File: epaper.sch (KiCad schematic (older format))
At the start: 6 parts, among them CON1 SD_Card, P1 USB_OTG, U1 ch340g, U2 LTC4080, U3 ESP-12E, U4 TCA8418RTWR

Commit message: keypad
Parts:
- added C?: 100nf, symbol C
- added C?: 10pF, symbol C
- added C? (x3): 4.7uf, symbol C
- added L?: NRG4026T100M, symbol INDUCTOR
- added R?: 10k, symbol R
- added R? (x2): 470, symbol R
- added R?: 806, symbol R
- added R? (x2): R, symbol R
- added R? (x3): 0, symbol R
- added SW? (x40): butt, symbol SW_PUSH_SMALL_H
- added Y?: 12mhz, symbol Crystal
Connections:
- net labels added: +3V3, +5V, +BATT, COL0, COL1, COL2, COL3, COL4, COL5, COL6, COL7, COL8, COL9, ROW0, ROW1, ROW2, ROW3, RXD0, SCL, SDA, TXD0
- wire segments 13 -> 144
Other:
- moved on the sheet: CON1, P1, U1, U2

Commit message: display conn and ltc4080
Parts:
- added C?: 100nf, symbol C
- added C?: 10uf, symbol C
- added P?: Sharp Memory LCD, symbol CONN_01X10
- added R?: 0, symbol R
- C?: value 10pF -> 10pf
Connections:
- net labels added: CS_LCD
- net labels removed: VCC
- wire segments 144 -> 244

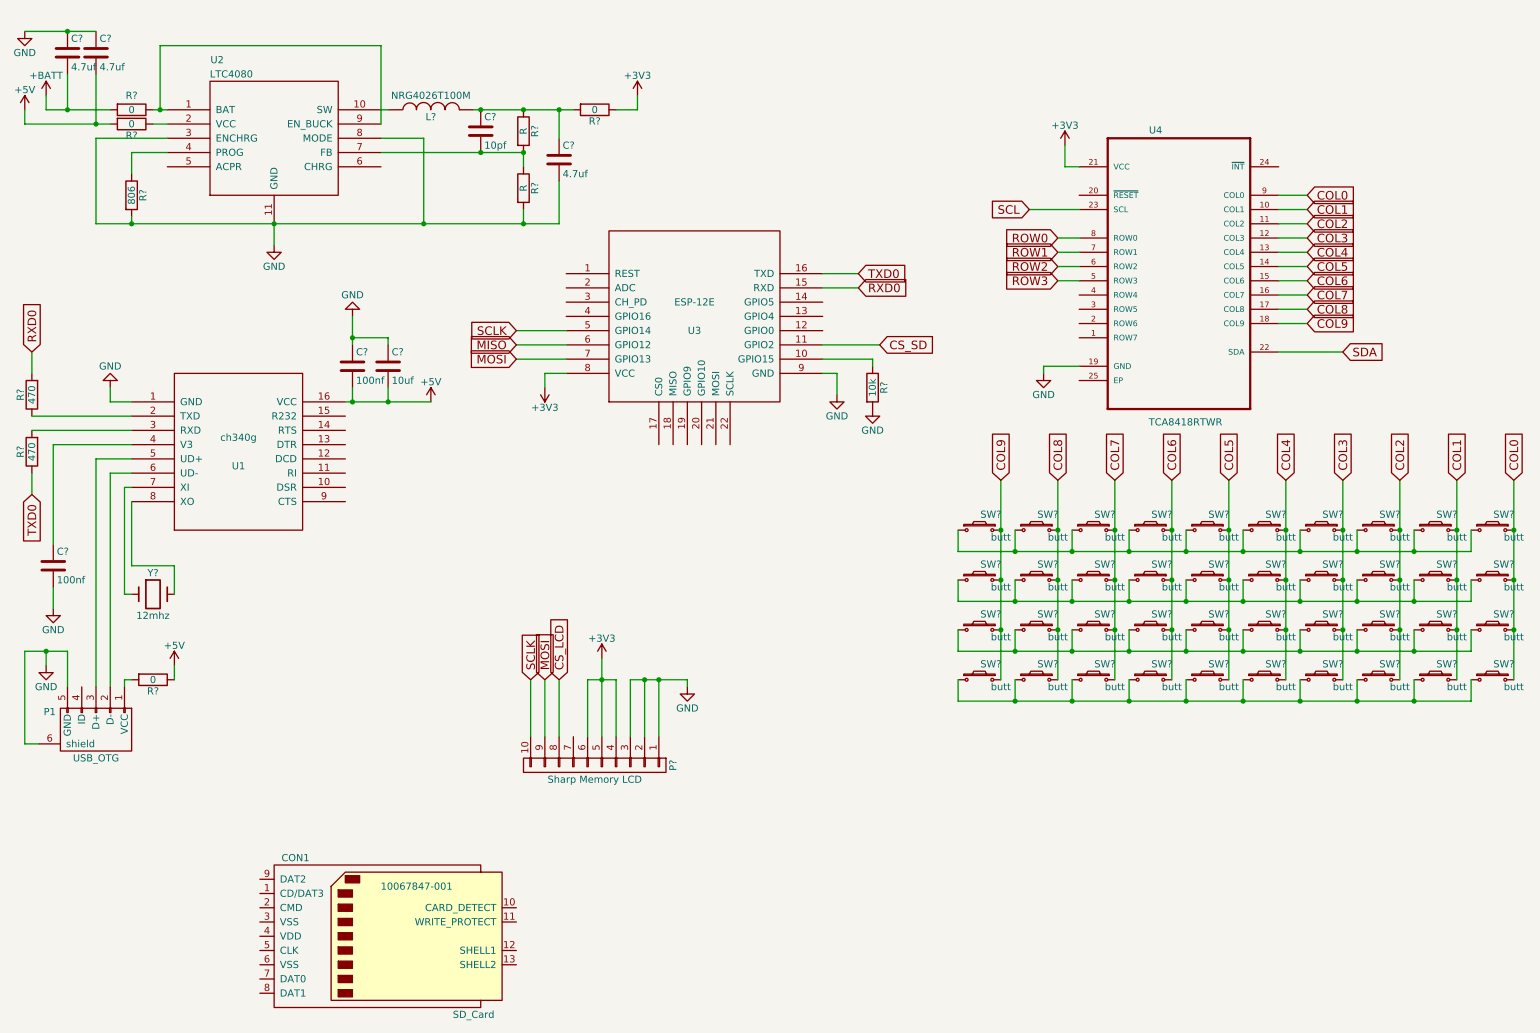
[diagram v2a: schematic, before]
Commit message: usb to rs232
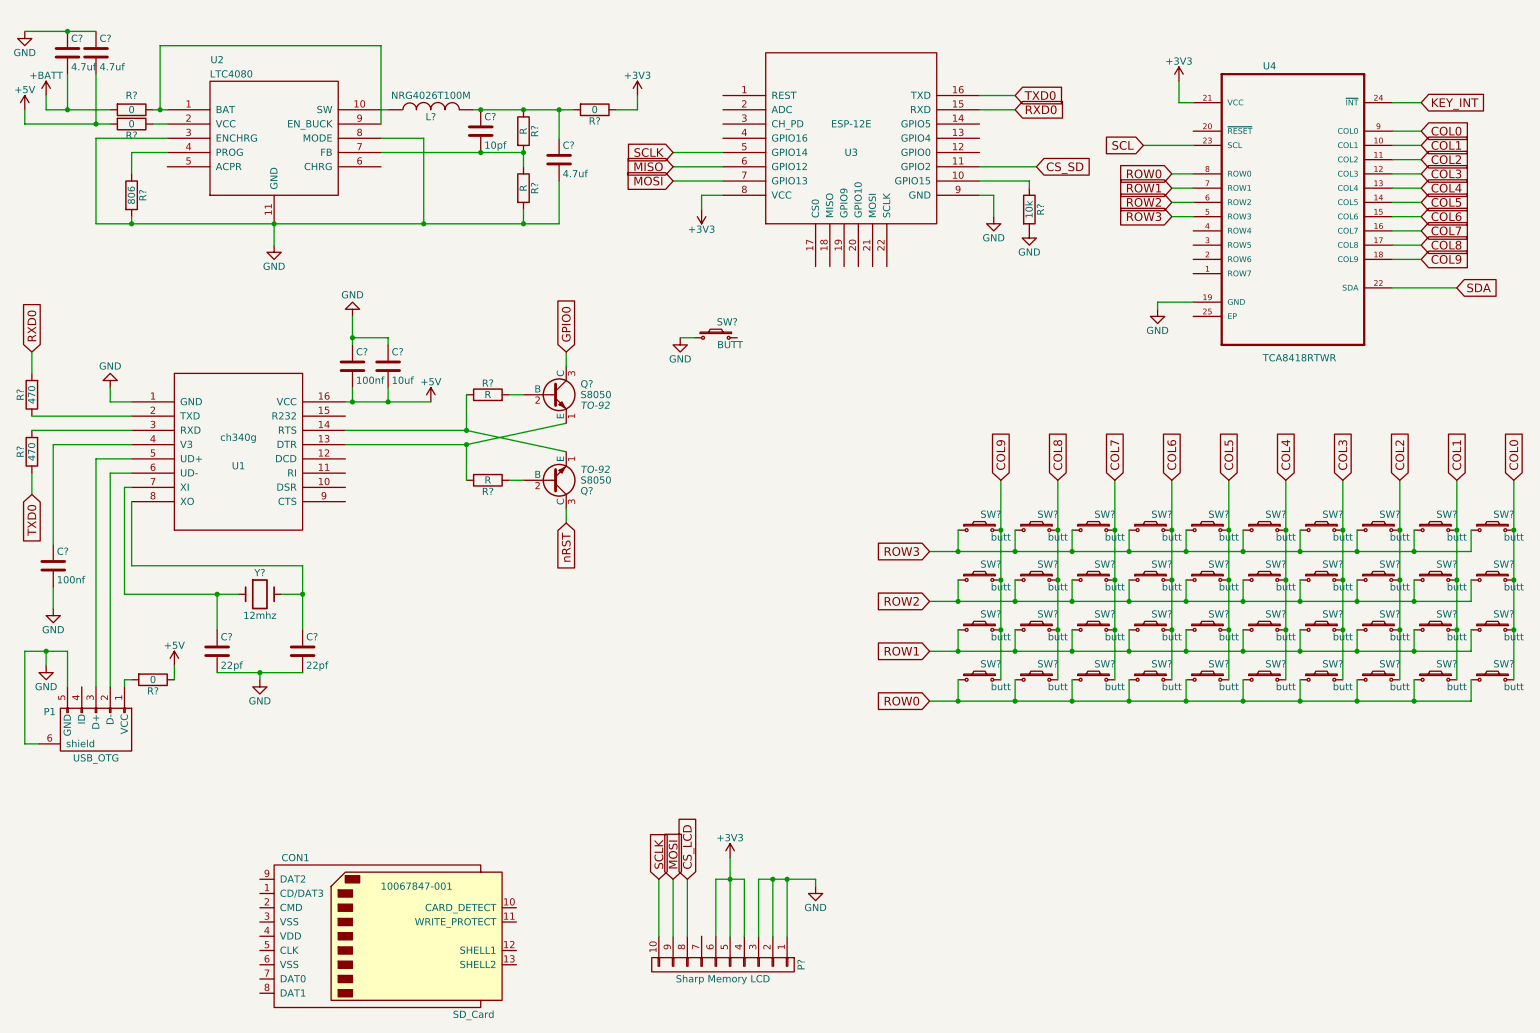
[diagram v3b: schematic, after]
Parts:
- added C? (x2): 22pf, symbol C
- added Q? (x2): S8050, TO-92, symbol S8050
- added R? (x2): R, symbol R
- added SW?: BUTT, symbol SW_PUSH_SMALL_H
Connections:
- net GND: now also C?.2, C?.2, SW?.1
- net ROW0: now also SW?.1, SW?.1, SW?.1, SW?.1, SW?.1, SW?.1, SW?.1, SW?.1, SW?.1, SW?.1
- net ROW1: now also SW?.1, SW?.1, SW?.1, SW?.1, SW?.1, SW?.1, SW?.1, SW?.1, SW?.1, SW?.1
- net ROW2: now also SW?.1, SW?.1, SW?.1, SW?.1, SW?.1, SW?.1, SW?.1, SW?.1, SW?.1, SW?.1
- net ROW3: now also SW?.1, SW?.1, SW?.1, SW?.1, SW?.1, SW?.1, SW?.1, SW?.1, SW?.1, SW?.1
- net KEY_INT: now reaches U4.24 (~INT)
- net at U1.13 (DTR): now also Q?.1 (E), R?.2
- net at U1.14 (RTS): now also Q?.1 (E), R?.1
- net at U1.7 (XI), Y?.1: now also C?.1
- net at U1.8 (XO), Y?.2: now also C?.1
- new net: Q?.2 (B), R?.2
- new net: Q?.2 (B), R?.1
- new net GPIO0: Q?.3 (C)
- new net nRST: Q?.3 (C)
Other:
- moved on the sheet: P?, R?, U3, U4, Y?

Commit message: before append new sheet
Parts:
- removed CON1: SD_Card, 10067847-001, symbol SD_Card
- added P?: microSD, symbol CONN_01X10
- added R?: 470, symbol R
- added R? (x2): 10k, symbol R
- added W? (x3): TP, symbol TEST_1P
- R? (x2): value R -> 12k
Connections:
- net +3V3: now also P?.4 (P4), R?.2, R?.2
- net CS_SD: now also P?.2 (P2)
- net GND: now also P?.6 (P6)
- net GPIO0: now also U3.12 (GPIO0), R?.1
- net MISO: now also P?.7 (P7)
- net MOSI: now also P?.3 (P3)
- net RXD0: now also W?.1
- net SCL: now also U3.14 (GPIO5), R?.1
- net SCLK: now also P?.5 (P5)
- net SDA: now also U3.13 (GPIO4), R?.1
- net TXD0: now also W?.1
- net nRST: now also U3.1 (REST), W?.1
- net at SW?.2: now also R?.2
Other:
- moved on the sheet: SW?

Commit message: updates
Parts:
- removed C?: 100nf, symbol C
- removed R?: 0, symbol R
- added D?: D_Schottky, symbol D_Schottky
- added P?: Battery, symbol CONN_01X02
- added R?: 0, symbol R
- added R? (x2): 10k, symbol R
- added SW?: SPST, symbol SPST
- added W?: TP_SCL, symbol TEST_1P
- added W?: TP_SDA, symbol TEST_1P
- added W?: TP_R, symbol TEST_1P
- W?: value TP -> TP_TX
- W?: value TP -> TP_RX
- W?: value TP -> TP_RST
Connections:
- net +3V3: now also C?.2, C?.2, U1.16 (VCC), U1.4 (V3), R?.2, R?.2
- net +5V: now also D?.1 (K); no longer C?.2, C?.2, U1.16 (VCC)
- net +BATT: now also SW?.1
- net CS_SD: now also R?.1
- net GND: now also P?.2 (P2)
- net SCL: now also W?.1
- net SDA: now also W?.1
- net at U4.20 (~RESET): now also W?.1
- net at P1.1 (VCC): now also D?.2 (A)
- net at U3.3 (CH_PD): now also R?.1
- new net: P?.1 (P1), R?.2
- new net: R?.1, SW?.2
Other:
- moved on the sheet: R?, W?

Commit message: annotate
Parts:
- C1, C2, C3, C4, C5, C6, C7, C8: renamed from C?; footprint (none) -> Capacitors_SMD:C_0603_HandSoldering
- P1: footprint (none) -> Connectors:USB_Micro-B
- R1, R10, R11, R12, R13, R14, R15, R16, R17, R2, R3, R4, R5, R6, R7, R8, R9: renamed from R?; footprint (none) -> Resistors_SMD:R_0603_HandSoldering
- gave numbers to parts that had none: 56

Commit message: reistor values, comments
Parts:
- added R18: 600k, symbol R
- added R19: 190k, symbol R
- R10: value R -> 600k
- R11: value R -> 190k
- R7, R8: value 12k -> 10k
- U1: footprint MODULE -> SMD_Packages:SO-16-N
- U3: footprint (none) -> ESP8266:ESP-12E
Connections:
- net +BATT: now also R19.1
- net GND: now also R18.2
- net at U3.2 (ADC): now also R18.1, R19.2
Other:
- note added: "Increase value of R5 if \nbattery is <500mAh. \nIcharge=400/R5"
- note added: "Power supply 3.3V @ 300mA\n"
- note added: "Vout=0.8*(1+R10/R11)\n"
- moved on the sheet: R13, W1

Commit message: footprints
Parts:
- P2: footprint (none) -> Connectors:PINHEAD1-2
- P4: footprint (none) -> 52892-1095:MOLEX_52892-1095
- Q1, Q2: footprint TO-92 -> TO_SOT_Packages_SMD:SOT-23_Handsoldering
- R18, R19: footprint (none) -> Resistors_SMD:R_0603_HandSoldering
- U2: footprint MODULE -> Housings_SSOP:MSOP-10-1EP_3x3mm_Pitch0.5mm
- U4: footprint QFN50P400X400X80-25N -> Housings_DFN_QFN:QFN-24-1EP_4x4mm_Pitch0.5mm
- W1, W2, W3, W4, W5, W6: footprint (none) -> Connectors:1pin
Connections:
- no-connect marks 0 -> 5
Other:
- note added: "-make sure to check "remove silscreen from soldermask areas" on export\n"
